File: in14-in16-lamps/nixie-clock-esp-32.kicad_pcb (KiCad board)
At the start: 2 copper layers, 153 x 50 mm, 90 parts, among them J1 Conn_01x02_Pin, J2 Conn_01x02_Pin, J3 Conn_01x06_Pin, J4 Conn_01x02_Pin, Q1 MMBTA42, Q10 2N7002, Q11 MMBTA42, Q12 MMBTA92, Q13 MMBTA42, Q14 MMBTA92, Q15 MMBTA42, Q2 MMBTA92, Q3 MMBTA42, Q4 MMBTA92, Q5 MMBTA42, Q6 MMBTA92, Q7 MMBTA42, Q8 MMBTA92, Q9 MMBTA42, SW1 SW_Push, U1 max688 boost regulator 5 to 1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, U2 AMS1117-3.3, U3 ESP32-WROOM-32D, U4 DS3231M, U5 74141

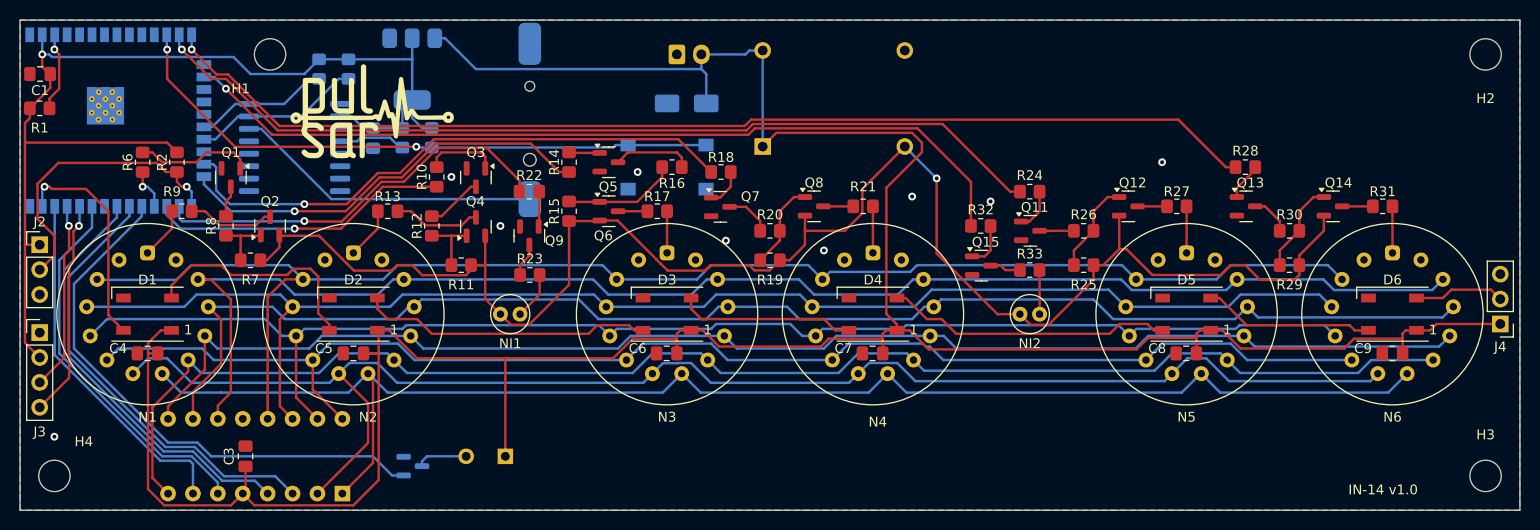
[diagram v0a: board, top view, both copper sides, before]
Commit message: add in-14 and in-16 6 lamp version
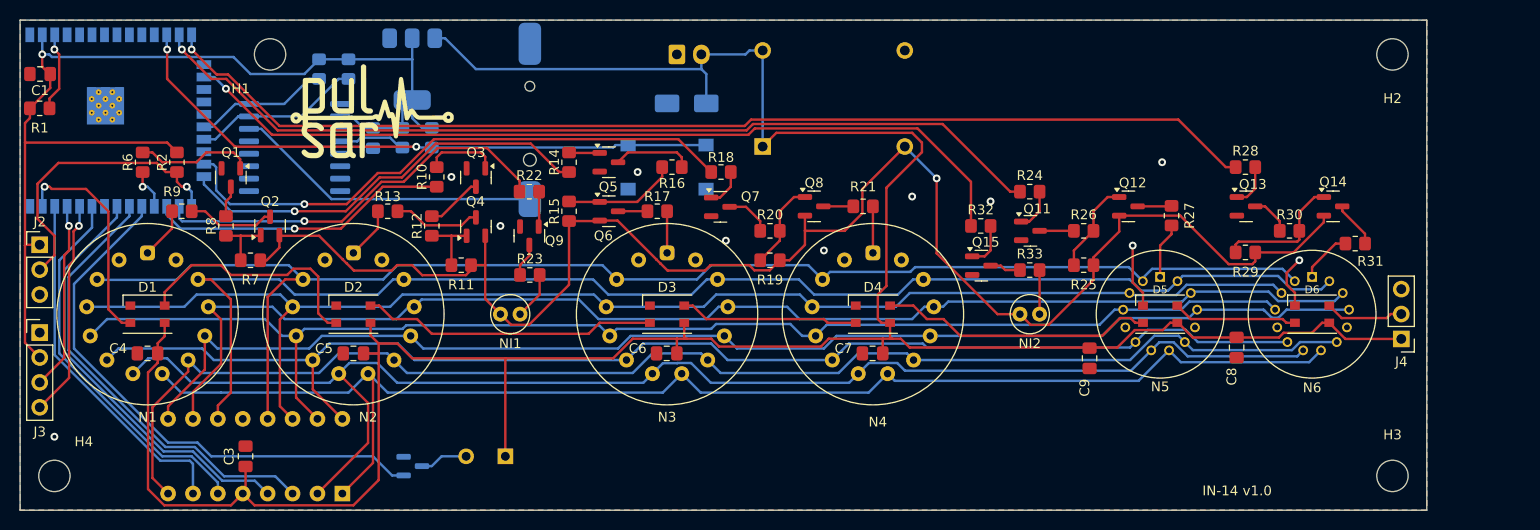
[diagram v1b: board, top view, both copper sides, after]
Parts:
- D1, D2, D3, D4, D5, D6: footprint LED_SMD:LED_WS2812B_PLCC4_5.0x5.0mm_P3.2mm -> project_library:SK6812_mini
- N5, N6: value IN-14 nixie tube -> IN-16 nixie tube; footprint project_library:IN-14_nixie_tube -> project_library:IN-16_nixie_tube
- moved C9 30.9 mm to (159.1, 84.5), turned to -90 degrees
- moved J4 10.2 mm to (190.9, 82.5)
- moved H2 9.50 mm to (190.0, 53.5)
- moved H3 9.50 mm to (190.0, 96.5)
- moved D6 8.20 mm to (181.8, 80.0)
- moved N6 8.20 mm to (181.8, 80.0)
- moved C8 5.17 mm to (174.1, 83.4), turned to -90 degrees
- moved R31 4.72 mm to (186.2, 72.8), turned to 0 degrees
- moved R29 4.68 mm to (175.0, 73.7)
- moved D5 2.70 mm to (166.3, 80.0)
- moved N5 2.70 mm to (166.3, 80.0)
- moved R27 1.09 mm to (167.5, 70.0), turned to 90 degrees
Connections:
- N5 pad 10: DIG8 -> unconnected-(N5-LC-Pad10)
- N5 pad 11: DIG9 -> DIG8
- N5 pad 12: DIG0 -> DIG9
- N5 pad 13: unconnected-(N5-RC-Pad13) -> DIG0
- N5 pad 2: unconnected-(N5-LC-Pad2) -> DIG1
- N5 pad 3: DIG1 -> DIG2
- N5 pad 4: DIG2 -> DIG3
- N5 pad 5: DIG3 -> unconnected-(N5-RC-Pad5)
- N6 pad 10: DIG8 -> unconnected-(N6-LC-Pad10)
- N6 pad 11: DIG9 -> DIG8
- N6 pad 12: DIG0 -> DIG9
- N6 pad 13: unconnected-(N6-RC-Pad13) -> DIG0
- N6 pad 2: unconnected-(N6-LC-Pad2) -> DIG1
- N6 pad 3: DIG1 -> DIG2
- N6 pad 4: DIG2 -> DIG3
- N6 pad 5: DIG3 -> unconnected-(N6-RC-Pad5)
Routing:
- net +5V: track 292.5 -> 279.2 mm
- net DIG9: track 146.4 -> 134.0 mm
- net GND: track 0.00 -> 12.1 mm, vias 9 -> 11
- net DIG0: track 149.5 -> 138.2 mm
- net DIG8: track 142.7 -> 132.2 mm
- net DIG7: track 150.3 -> 139.9 mm
- net DIG6: track 148.7 -> 139.3 mm
- net DIG5: track 151.5 -> 143.2 mm
- net DIG4: track 140.8 -> 133.6 mm
- net DIG2: track 145.0 -> 138.9 mm
- net DIG3: track 142.0 -> 135.8 mm
- net DIG1: track 149.8 -> 144.9 mm
- net Net-(D5-DOUT): track 17.5 -> 12.7 mm
- net Net-(Q14-B): track 9.43 -> 13.2 mm
- net HV: track 167.3 -> 164.8 mm
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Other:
- board size 153 x 50 mm -> 143.5 x 50 mm

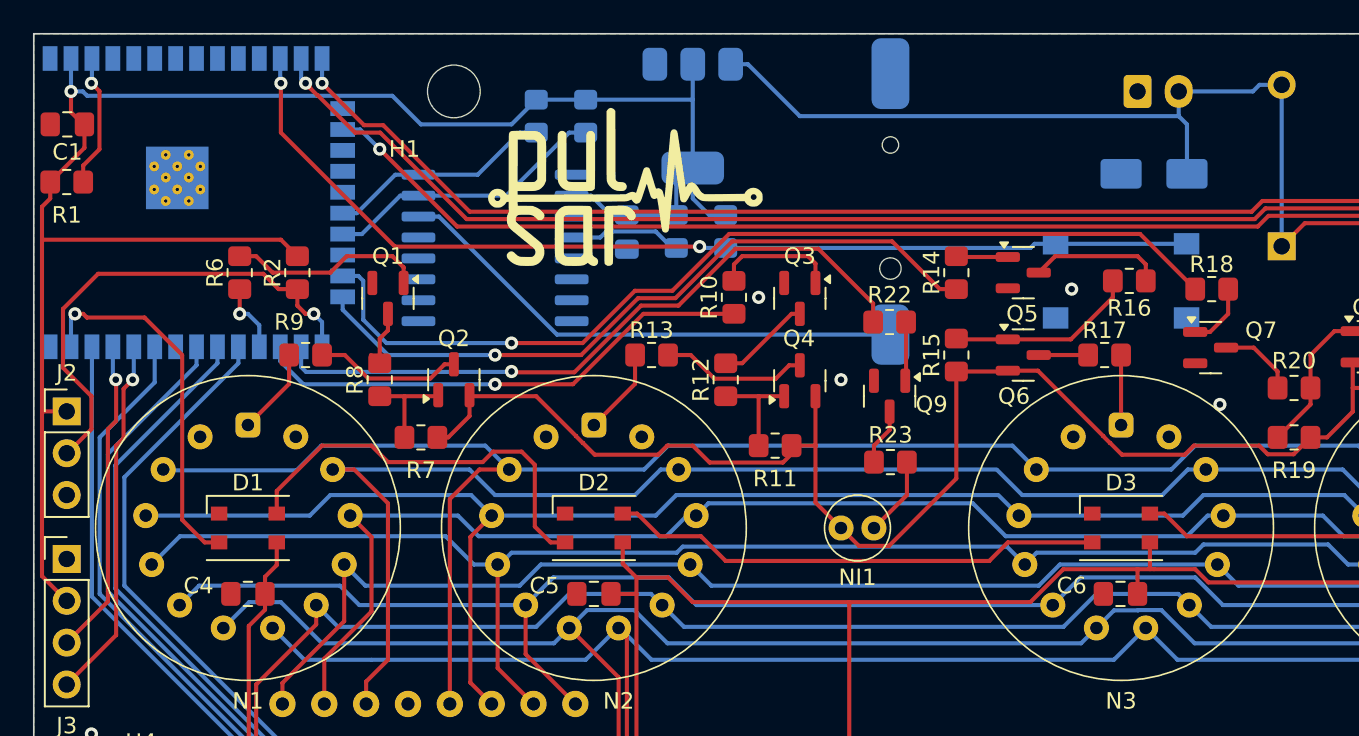
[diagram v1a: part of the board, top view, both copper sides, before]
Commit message: fix i2c connection
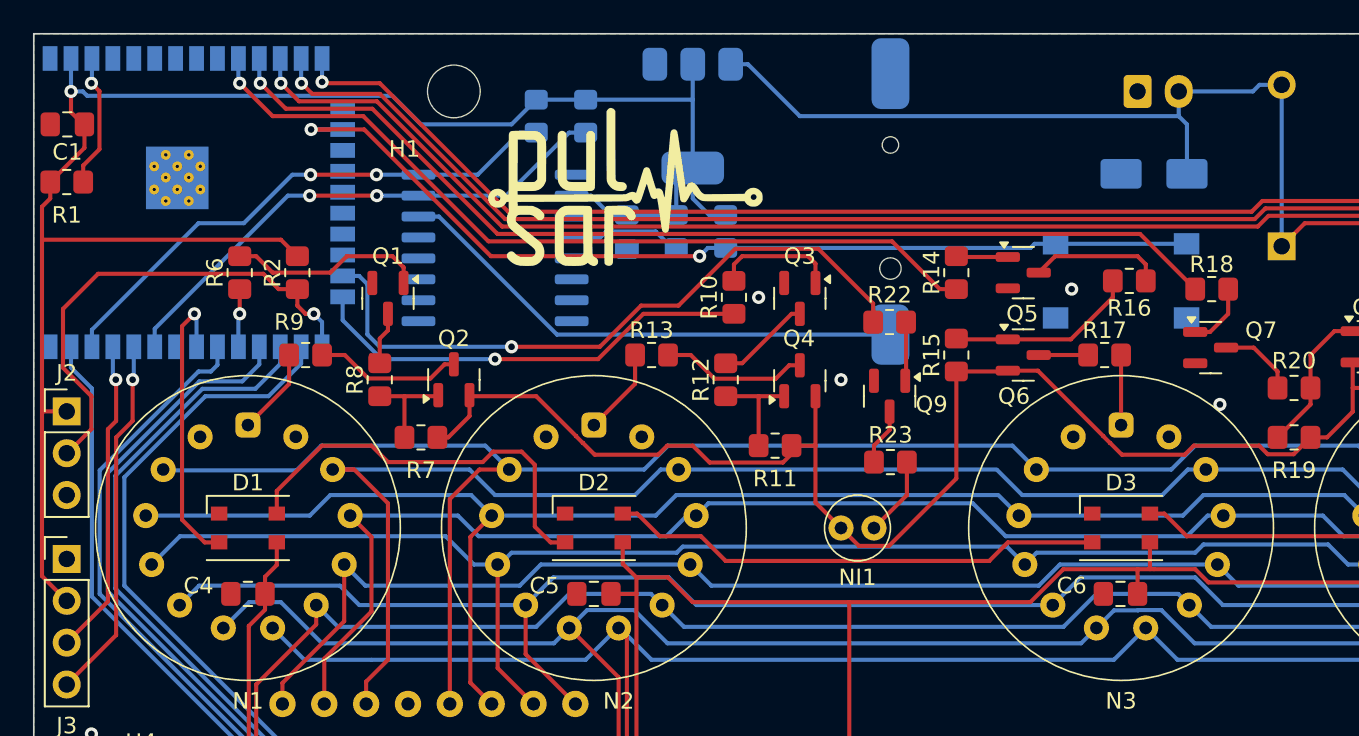
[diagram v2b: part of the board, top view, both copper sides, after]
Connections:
- U3 pad 10: unconnected-(U3-IO25-Pad10) -> A3
- U3 pad 11: unconnected-(U3-IO26-Pad11) -> A4
- U3 pad 12: /control/BTN2 -> IN2
- U3 pad 16: IN2 -> /control/BTN2
- U3 pad 20: /control/SCK -> unconnected-(U3-SCK/CLK-Pad20)
- U3 pad 21: /control/SDA -> unconnected-(U3-SDO/SD0-Pad21)
- U3 pad 23: A4 -> IN1
- U3 pad 24: A3 -> A2
- U3 pad 26: IN1 -> /control/BUZZ
- U3 pad 27: A2 -> DEC0
- U3 pad 28: A1 -> DEC3
- U3 pad 29: /control/BUZZ -> A1
- U3 pad 30: DEC0 -> DEC1
- U3 pad 31: DEC3 -> WS2812
- U3 pad 33: DEC1 -> /control/SDA
- U3 pad 36: DEC2 -> /control/SCK
- U3 pad 37: WS2812 -> DEC2
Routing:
- net /control/SCK: track 13.8 -> 33.1 mm, vias 0 -> 2
- net /control/SDA: track 17.3 -> 32.3 mm, vias 0 -> 2
- net A3: track 43.2 -> 50.2 mm
- net IN2: track 87.7 -> 94.1 mm
- net WS2812: track 22.5 -> 17.7 mm
- net A4: track 59.0 -> 63.5 mm
- net /control/BTN2: track 62.5 -> 58.6 mm
- net /control/BUZZ: track 56.5 -> 60.2 mm
- net A2: track 30.8 -> 27.3 mm
- net DEC0: track 46.1 -> 49.6 mm
- net DEC3: track 43.8 -> 46.9 mm
- net DEC1: track 39.1 -> 41.2 mm
- net IN1: track 41.7 -> 40.7 mm
- net A1: track 4.29 -> 3.53 mm
- net DEC2: track 36.9 -> 37.4 mm
